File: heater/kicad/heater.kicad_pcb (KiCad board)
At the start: 2 copper layers, 90 x 88.4 mm, 117 parts, among them J1 Conn_01x07_Pin, J2 Conn_01x02_Pin, J3 Conn_01x02_Pin, J4 Conn_01x02_Pin, J5 pcie_98, U1 ADS1261BIRHBT, U2 ESD5344D-TP, U3 TPS7A2050PDBVR, U4 TPS7A2025PDBVRr, U6 TPS65135, U7 ADP7182AUJZ-5.0, U8 ADP7182AUJZ-2.5, U9 XC6206P332MR

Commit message: Heater PCB layout in progress.
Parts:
- removed C19: 220n, Capacitor_SMD:C_0402_1005Metric
- removed C22, C29, C32, C33, C37, C40, C41, C42, C47, C48: 10u, Capacitor_SMD:C_0603_1608Metric
- removed C23, C24, C25, C30, C31, C34, C36, C38, C39, C43, C44: 100n, Capacitor_SMD:C_0402_1005Metric
- removed C35, C45, C46: 1u, Capacitor_SMD:C_0402_1005Metric
- removed D3, D4: GRN, LED_SMD:LED_0603_1608Metric
- removed J3, J4: Conn_01x02_Pin, heater:connector_2pins_horizontal
- removed JP1, JP2: SolderJumper_2_Bridged, Jumper:SolderJumper-2_P1.3mm_Bridged_Pad1.0x1.5mm
- removed L1: 2u2H, heater:Inductor_C329578
- removed R1, R12, R2, R30, R36, R37, R38, R39, R40, R41, R42: 2K 0.1%, Resistor_SMD:R_0402_1005Metric
- removed R11, R20, R34, R5, R6: 1K, Resistor_SMD:R_0402_1005Metric
- removed R18, R19, R21: 47R, Resistor_SMD:R_0402_1005Metric
- removed R23, R24: 10K, Resistor_SMD:R_0402_1005Metric
- removed R25, R26: 5K1, Resistor_SMD:R_0402_1005Metric
- removed R28, R29: 51K, Resistor_SMD:R_0402_1005Metric
- removed R31: 360K 1%, Resistor_SMD:R_0402_1005Metric
- removed R32: 100K 1%, Resistor_SMD:R_0402_1005Metric
- removed R33: 464K 1%, Resistor_SMD:R_0402_1005Metric
- removed TP6: TestPoint, common:Test_Pad
- removed U6: TPS65135, heater:WQFN-16-1EP_3x3mm_P0.5mm_EP1.68x1.68mm_ThermalVias
- added R14: 0R, Resistor_SMD:R_0402_1005Metric, F.Cu at (77.4, -44.4)
- added R17: 30K, Resistor_SMD:R_0402_1005Metric, F.Cu at (77.4, -38.4)
- added TP10: TestPoint, common:Test_Pad, F.Cu at (83.2, -38.1)
- added TP11: TestPoint, common:Test_Pad, F.Cu at (83.2, -35.2)
- added TP12: TestPoint, common:Test_Pad, F.Cu at (86.1, -43.9)
- added TP13: TestPoint, common:Test_Pad, F.Cu at (86.1, -41.0)
- added TP14: TestPoint, common:Test_Pad, F.Cu at (86.1, -38.1)
- added U14: OPA863DBVR, heater:SOT-23-5, F.Cu at (70.4, -48.1)
- added U16: OPA863DBVR, heater:SOT-23-5, F.Cu at (70.4, -43.6)
- added U5: ISO1541, Package_SO:SOIC-8_3.9x4.9mm_P1.27mm, F.Cu at (91.8, -32.3)
- C1: value 2u2 -> 10u; footprint Capacitor_SMD:C_0402_1005Metric -> Capacitor_SMD:C_0603_1608Metric
- C10, C11: value 1u -> 100n
- C13: value 100n -> 2u2; footprint Capacitor_SMD:C_0402_1005Metric -> Capacitor_SMD:C_0805_2012Metric
- C14: value 22n -> 10u; footprint Capacitor_SMD:C_0402_1005Metric -> Capacitor_SMD:C_0603_1608Metric
- C15: value 220n -> 100n
- C16, C18: value 22n -> 100n
- C17: value 4n7 -> 100n
- C20: value 22n -> 10n
- C21: value 1u -> 10u; footprint Capacitor_SMD:C_0402_1005Metric -> Capacitor_SMD:C_0603_1608Metric
- C26: value 10u -> 10u 16V
- C4: value 100n -> 10u; footprint Capacitor_SMD:C_0402_1005Metric -> Capacitor_SMD:C_0603_1608Metric
- C5: footprint Capacitor_SMD:C_0402_1005Metric -> Capacitor_SMD:C_0805_2012Metric
- C6: value 2u2 -> 100n
- C9: value 100n -> 10u 16V; footprint Capacitor_SMD:C_0402_1005Metric -> Capacitor_SMD:C_0603_1608Metric
- D1: value GRN -> RED
- D2: value GRN -> YEL
- J1: value Conn_01x07_Pin -> Conn_01x02_Pin; footprint heater:connector_7pins_horizontal -> Connector_JST:JST_VH_B2PS-VH_1x02_P3.96mm_Horizontal
- J2: footprint heater:connector_2pins_horizontal -> Connector_JST:JST_VH_B2PS-VH_1x02_P3.96mm_Horizontal
- R10, R9: value 1K -> 1K8
- R13: value 2K 0.1% -> 0R
- R15: value 51K -> 3K3
- R16: value 51K -> 0R
- R22: value 47R -> 5K1
- R3: value 2K 0.1% -> 30K
- R4: value 1K -> 0R025 50ppm 3W; footprint Resistor_SMD:R_0402_1005Metric -> Resistor_SMD:R_2512_6332Metric
- R7, R8: value 2K 0.1% -> 1K8
- U1: value ADS1261BIRHBT -> OPA863DBVR; footprint heater:RHB0032E -> heater:SOT-23-5
- U3: value TPS7A2050PDBVR -> LP2985-5.0; footprint heater:SOT-23-5 -> Package_TO_SOT_SMD:SOT-23-5
- U4: value TPS7A2025PDBVRr -> ESD5344D-TP; footprint heater:SOT-23-5 -> common:Diodes_UDFN-10_1.0x2.5mm_P0.5mm
- U7: value ADP7182AUJZ-5.0 -> OPA863DBVR; footprint Package_TO_SOT_SMD:TSOT-23-5 -> heater:SOT-23-5
- U8: value ADP7182AUJZ-2.5 -> ADS1115IDGS; footprint Package_TO_SOT_SMD:TSOT-23-5 -> Package_SO:TSSOP-10_3x3mm_P0.5mm
- U9: footprint Package_TO_SOT_SMD:SOT-23-3 -> Package_TO_SOT_SMD:SOT-89-3
- moved D2 121.5 mm to (98.2, -38.0), turned to 0 degrees
- moved TP8 105.5 mm to (83.2, -43.9)
- moved U8 100.6 mm to (82.3, -31.4), turned to 0 degrees
- moved TP2 95.8 mm to (80.3, -43.9)
- moved U9 95.8 mm to (99.4, -32.5), turned to 0 degrees
- moved C18 92.5 mm to (94.7, -42.4), turned to 0 degrees
- moved TP4 92.4 mm to (80.3, -38.1)
- moved TP5 90.5 mm to (80.3, -35.2)
- moved C17 90.1 mm to (94.7, -44.4), turned to 0 degrees
- moved C15 89.9 mm to (91.8, -38.5)
- moved C12 89.3 mm to (91.8, -40.4), turned to 0 degrees
- moved C10 89.3 mm to (91.8, -44.4), turned to 0 degrees
- moved C16 89.1 mm to (91.8, -36.5), turned to 0 degrees
- moved C20 88.5 mm to (94.7, -40.4), turned to 0 degrees
- moved C14 88.1 mm to (94.8, -54.9), turned to 0 degrees
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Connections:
- C1 pad 1: /AIN6 -> GND
- C1 pad 2: /AIN7 -> +5V
- C10 pad 2: /+2V5A -> +3V3
- C11 pad 1: /+3V3D -> +5VF
- C11 pad 2: GND -> GND1
- C12 pad 1: GND -> +5VF
- C12 pad 2: /+2V5A -> GND1
- C13 pad 1: /+3V3D -> GND1
- C13 pad 2: GND -> Net-(U6-OUT)
- C14 pad 1: /AIN2 -> GND
- C14 pad 2: GND -> +5V
- C15 pad 1: /AIN0 -> +5VF
- C15 pad 2: /AIN1 -> GND1
- C16 pad 1: GND -> +5VF
- C16 pad 2: /AIN1 -> GND1
- C17 pad 1: Net-(U1-CAPN) -> +5VF
- C17 pad 2: Net-(U1-CAPP) -> GND1
- C18 pad 1: /AIN0 -> GND
- C18 pad 2: GND -> +5V
- C2 pad 2: /AIN6 -> +5V
- C20 pad 1: GND -> GND1
- C20 pad 2: /AIN3 -> Net-(U3-BP)
- C21 pad 1: Net-(U1-BYPASS) -> GND1
- C21 pad 2: GND -> +5VF
- C26 pad 1: GND -> GND1
- C26 pad 2: /+5VA -> /9VF
- C27 pad 1: GND -> GND1
- C27 pad 2: /+2V5A -> +5VF
- C28 pad 1: GND -> GND1
- C28 pad 2: /+2V5A -> +5VF
- C3 pad 2: /AIN4 -> +3V3
- C4 pad 1: /AIN7 -> GND
- C4 pad 2: GND -> +3V3
- C5 pad 1: /AIN8 -> GND1
- C5 pad 2: /AIN9 -> Net-(U15-OUT)
- C6 pad 1: /AIN4 -> +5VF
- C6 pad 2: /AIN5 -> GND1
- C7 pad 1: GND -> +5VF
- C7 pad 2: /AIN8 -> GND1
- C8 pad 1: /AIN9 -> +5VF
- C8 pad 2: GND -> GND1
- C9 pad 1: /AIN5 -> GND1
- C9 pad 2: GND -> /9VF
- D1 pad 1: GND -> Net-(D1-K)
- D1 pad 2: Net-(D1-A) -> +5VF
- D2 pad 1: Net-(D2-K) -> GND
- D2 pad 2: GND -> Net-(D2-A)
- D5 pad 1: GND -> GND1
- J1 pad 1: /-5VA -> GND1
- J2 pad 2: Net-(J2-Pin_2) -> Net-(J1-Pin_2)
- J5 pad A16: /PB14 -> unconnected-(J5-Pin_a16-PadA16)
- J5 pad A27: /PA7 -> unconnected-(J5-Pin_a27-PadA27)
- J5 pad B1: +5VD -> +5V
- J5 pad B10: unconnected-(J5-Pin_b10-PadB10) -> /PB7
- J5 pad B12: unconnected-(J5-Pin_b12-PadB12) -> /PB8
- J5 pad B2: +5VD -> +5V
- J5 pad B21: /PA6 -> unconnected-(J5-Pin_b21-PadB21)
- J5 pad B28: /PA5 -> unconnected-(J5-Pin_b28-PadB28)
- J5 pad B3: +5VD -> +5V
- J5 pad B4: +5VD -> +5V
- R10 pad 1: Net-(J4-Pin_2) -> /PB8
- R10 pad 2: /AIN8 -> +3V3
- R13 pad 1: /AIN0 -> Net-(U8-ADDR)
- R13 pad 2: Net-(J1-Pin_6) -> Net-(U5-SCL2)
- R15 pad 1: /PA6 -> +3V3
- R15 pad 2: /+3V3D -> Net-(D2-A)
- R16 pad 1: /PB14 -> Net-(U8-ADDR)
- R16 pad 2: /+3V3D -> GND1
- R22 pad 1: /PB14 -> Net-(R22-Pad1)
- R22 pad 2: Net-(U1-CS_N) -> Net-(D1-K)
- R27 pad 1: /+3V3D -> +5VF
- R3 pad 1: Net-(J2-Pin_2) -> Net-(U16--)
- R3 pad 2: /+2V5A -> Net-(U8-AIN1)
- R4 pad 1: Net-(J3-Pin_2) -> GND1
- R4 pad 2: /AIN6 -> Net-(J2-Pin_1)
- R7 pad 1: Net-(J4-Pin_2) -> Net-(U5-SDA2)
- R7 pad 2: /+2V5A -> +5VF
- R8 pad 1: /-2V5A -> Net-(U5-SCL2)
- R8 pad 2: Net-(J4-Pin_1) -> +5VF
- R9 pad 1: Net-(J2-Pin_1) -> /PB7
- R9 pad 2: /AIN5 -> +3V3
- TP2 pad 1: +5VD -> +3V3
- TP3 pad 1: /+5V7 -> Net-(U8-AIN1)
- TP4 pad 1: /-5V7 -> /9VF
- TP5 pad 1: /+5VA -> Net-(U15-OUT)
- TP7 pad 1: /+2V5A -> +5VF
- TP8 pad 1: /-2V5A -> Net-(U14-+)
- TP9 pad 1: /+3V3D -> Net-(R22-Pad1)
- U1 pad 1: GND -> Net-(R22-Pad1)
- U1 pad 2: Net-(U1-CAPP) -> GND1
- U1 pad 3: Net-(U1-CAPN) -> Net-(U1-+)
- U1 pad 4: /+2V5A -> Net-(U1--)
- U1 pad 5: /-2V5A -> +5VF
- U2 pad 1: /PB14 -> /PB7
- U2 pad 2: /PA6 -> unconnected-(U2-D2-Pad2)
- U2 pad 4: /PA7 -> unconnected-(U2-D3-Pad4)
- U2 pad 5: /PA5 -> /PB8
- U3 pad 1: /+5V7 -> /9VF
- U3 pad 2: GND -> GND1
- U3 pad 3: /+5V7 -> /9VF
- U3 pad 4: unconnected-(U3-NC-Pad4) -> Net-(U3-BP)
- U3 pad 5: /+5VA -> +5VF
- U4 pad 1: /+5VA -> +5V
- U4 pad 2: GND -> +5V
- U4 pad 3: /+5VA -> GND
- U4 pad 5: /+2V5A -> unconnected-(U4-D4-Pad5)
- U7 pad 1: GND -> Net-(U8-AIN0)
- U7 pad 2: /-5V7 -> GND1
- U7 pad 3: /-5V7 -> Net-(U6-OUT)
- U7 pad 4: unconnected-(U7-NC-Pad4) -> Net-(U7--)
- U7 pad 5: /-5VA -> +5VF
- U8 pad 1: GND -> Net-(U8-ADDR)
- U8 pad 2: /-5VA -> unconnected-(U8-RDY-Pad2)
- U8 pad 3: /-5VA -> GND1
- U8 pad 4: unconnected-(U8-NC-Pad4) -> Net-(U8-AIN0)
- U8 pad 5: /-2V5A -> Net-(U8-AIN1)
- U9 pad 2: /+3V3D -> +3V3
- U9 pad 3: +5VD -> +5V
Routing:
- net /-2V5A: track 151.7 -> 0.00 mm, vias 8 -> 0
- net /+2V5A: track 145.5 -> 0.00 mm, vias 3 -> 0
- net /+3V3D: track 142.6 -> 0.00 mm, vias 4 -> 0
- net /-5VA: track 99.1 -> 0.00 mm, vias 2 -> 0
- net +5VD: track 93.2 -> 0.00 mm
- net GND: track 121.2 -> 32.8 mm, vias 45 -> 0
- net /+5VA: track 76.4 -> 0.00 mm, vias 2 -> 0
- net /PA5: track 62.3 -> 0.00 mm, vias 2 -> 0
- net /PA7: track 60.7 -> 0.00 mm, vias 3 -> 0
- net /PA6: track 60.2 -> 0.00 mm, vias 2 -> 0
- net /PB14: track 56.2 -> 0.00 mm, vias 1 -> 0
- net /AIN9: track 43.5 -> 0.00 mm
- net /AIN8: track 42.0 -> 0.00 mm
- net /+5V7: track 41.4 -> 0.00 mm
- net /-5V7: track 36.1 -> 0.00 mm, vias 2 -> 0
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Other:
- board text added: "PWM POWER VER 0.2"
- board text added: "locked"
- board text removed: "+2.5VA"
- board text removed: "+2V5A"
- board text removed: "+3.3VD"
- board text removed: "+3V3"
- board text removed: "+5.7V"
- board text removed: "+5VA"
- board text removed: "+5VD"
- board text removed: "-2.5VA"
- board text removed: "-2V5A"
- board text removed: "-5.7V"
- board text removed: "-5VA"
- board text removed: "ADC VER 0.2"
- board text removed: "LOAD CELL"

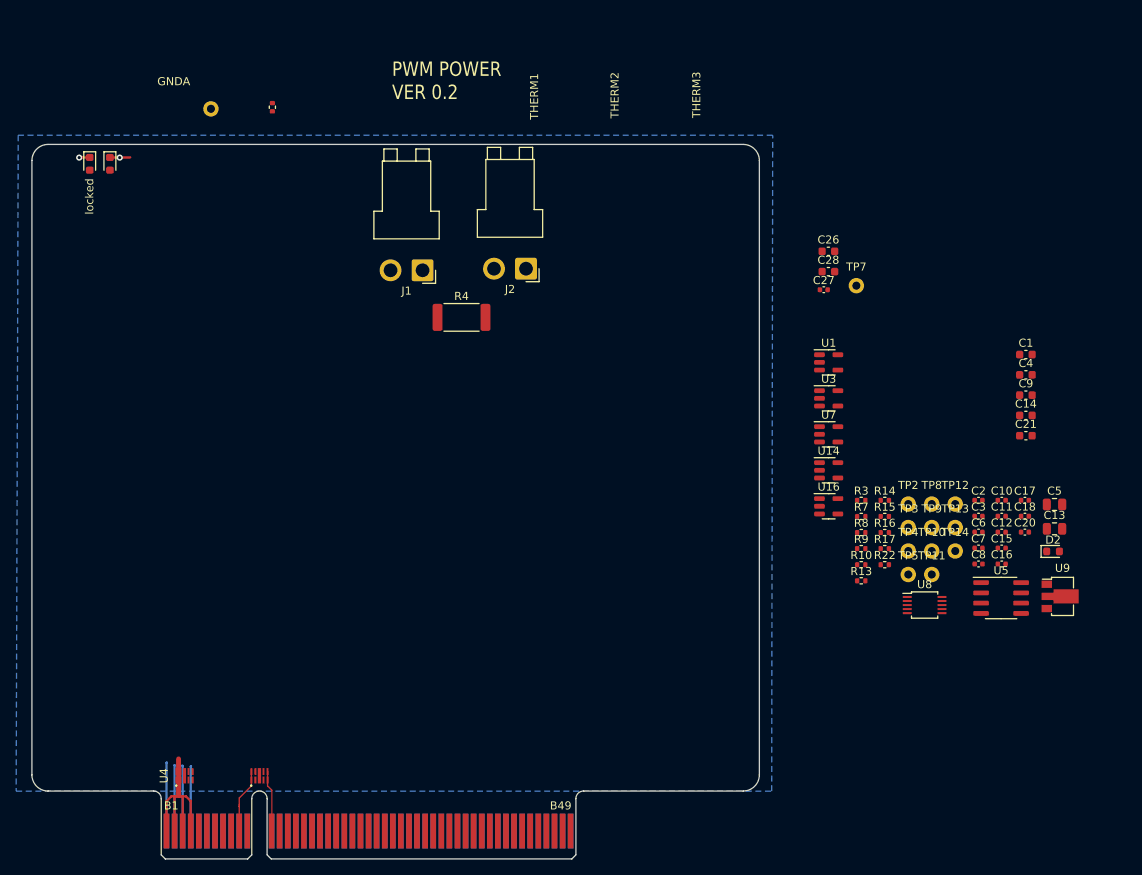
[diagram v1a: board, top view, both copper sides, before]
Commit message: Heater layout work in progress.
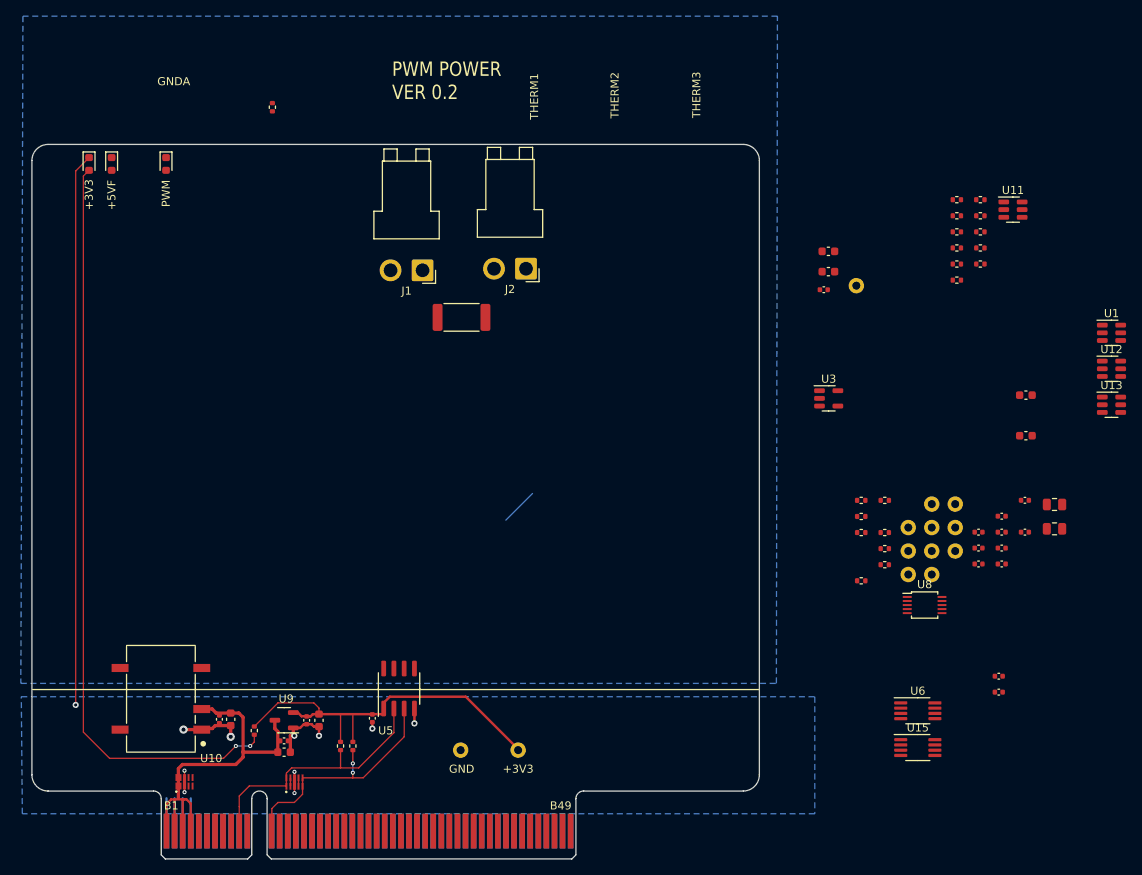
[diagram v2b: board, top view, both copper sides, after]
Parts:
- removed U14, U16, U7: OPA863DBVR, heater:SOT-23-5
- added C19: 100n 16V, Capacitor_SMD:C_0402_1005Metric, F.Cu at (91.5, -22.6)
- added C24: 100n 16V, Capacitor_SMD:C_0402_1005Metric, F.Cu at (91.5, -20.6)
- added R1: 10K, Resistor_SMD:R_0402_1005Metric, F.Cu at (86.3, -81.6)
- added R11: 50K, Resistor_SMD:R_0402_1005Metric, F.Cu at (86.3, -73.6)
- added R12: 2K, Resistor_SMD:R_0402_1005Metric, F.Cu at (86.3, -71.6)
- added R18: 10K, Resistor_SMD:R_0402_1005Metric, F.Cu at (89.2, -81.6)
- added R19: 100k, Resistor_SMD:R_0402_1005Metric, F.Cu at (89.2, -79.6)
- added R2: 1K, Resistor_SMD:R_0402_1005Metric, F.Cu at (86.3, -79.6)
- added R20: 3K3, Resistor_SMD:R_0402_1005Metric, F.Cu at (89.2, -77.6)
- added R21: 10K, Resistor_SMD:R_0402_1005Metric, F.Cu at (89.2, -75.6)
- added R24: 1M, Resistor_SMD:R_0402_1005Metric, F.Cu at (89.2, -73.6)
- added R5: 10K, Resistor_SMD:R_0402_1005Metric, F.Cu at (86.3, -77.6)
- added R6: 0R, Resistor_SMD:R_0402_1005Metric, F.Cu at (86.3, -75.6)
- added U10: B0509XT-1WR3, heater:Converter_DCDC, F.Cu at (-12.2, -19.8)
- added U11: OPA863SIDBVR, Package_TO_SOT_SMD:TSOT-23-6, F.Cu at (93.2, -80.3)
- added U12: OPA863SIDBVR, Package_TO_SOT_SMD:TSOT-23-6, F.Cu at (105.4, -60.6)
- added U13: OPA863SIDBVR, Package_TO_SOT_SMD:TSOT-23-6, F.Cu at (105.4, -56.2)
- added U15: LTC1968, Package_SO:MSOP-8_3x3mm_P0.65mm, F.Cu at (81.5, -13.8)
- added U6: LTC1968, Package_SO:MSOP-8_3x3mm_P0.65mm, F.Cu at (81.5, -18.3)
- D2: value YEL -> GRN
- J1, J2: footprint Connector_JST:JST_VH_B2PS-VH_1x02_P3.96mm_Horizontal -> heater:JST_VH_B2PS-VH_1x02_P3.96mm_Horizontal
- U1: value OPA863DBVR -> OPA863SIDBVR; footprint heater:SOT-23-5 -> Package_TO_SOT_SMD:TSOT-23-6
- U9: footprint Package_TO_SOT_SMD:SOT-89-3 -> heater:SOT-23-3
- moved D2 128.5 mm to (-21.1, -86.0), turned to -90 degrees
- moved C14 105.3 mm to (-3.56, -17.3), turned to 90 degrees
- moved C1 104.1 mm to (3.05, -13.2), turned to 180 degrees
- moved C18 102.8 mm to (-4.95, -17.3), turned to 90 degrees
- moved U9 97.5 mm to (3.05, -17.2), turned to 180 degrees
- moved C4 97.3 mm to (7.37, -17.1), turned to 90 degrees
- moved C2 90.9 mm to (3.05, -14.6), turned to 180 degrees
- moved C3 86.9 mm to (5.84, -17.1), turned to 90 degrees
- moved TP1 85.1 mm to (24.9, -13.5)
- moved C10 82.4 mm to (14.0, -17.4), turned to 90 degrees
- moved R15 82.4 mm to (-0.64, -15.9), turned to -90 degrees
- moved U5 75.3 mm to (17.3, -21.1), turned to 90 degrees
- moved R9 68.9 mm to (10.0, -14.0), turned to 90 degrees
- moved R10 66.8 mm to (11.6, -14.0), turned to 90 degrees
- moved TP2 57.1 mm to (32.0, -13.5)
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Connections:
- net GND1 renamed GNDF
- TP12 pad 1: Net-(U1--) -> Net-(U11--)
- TP8 pad 1: Net-(U14-+) -> Net-(U1-+)
- U1 pad 1: Net-(R22-Pad1) -> Net-(R1-Pad1)
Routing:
- net Net-(D2-A): track 0.00 -> 94.0 mm, vias 0 -> 2
- net GND: track 32.8 -> 107.9 mm, vias 0 -> 11
- net +3V3: track 0.00 -> 49.1 mm
- net /PB7: track 8.28 -> 32.9 mm
- net +5V: track 24.9 -> 49.6 mm
- net /PB8: track 7.58 -> 30.9 mm, vias 0 -> 2
- net GNDF: track 1.28 -> 4.67 mm, vias 1 -> 0
- net Net-(D1-K): track 2.50 -> 0.00 mm, vias 1 -> 0
- net unconnected-(U2-D3-Pad4): track 0.00 -> 1.05 mm
- net unconnected-(U2-D2-Pad2): track 0.00 -> 1.05 mm
- added copper zone on B.Cu, net GNDF
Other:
- board text added: "+3V3"
- board text added: "+5VF"
- board text added: "GND"
- board text added: "PWM"
- board text removed: "locked"

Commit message: More progress with the heater layout.
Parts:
- J1, J2: footprint heater:JST_VH_B2PS-VH_1x02_P3.96mm_Horizontal -> heater:JST_VH_2_CHINESE
- moved C9 110.3 mm to (-11.8, -29.2), turned to 180 degrees
- moved C24 104.3 mm to (-11.8, -35.4), turned to 180 degrees
- moved C20 103.8 mm to (-9.02, -37.8), turned to -90 degrees
- moved C19 103.4 mm to (-11.8, -27.6), turned to 180 degrees
- moved U13 98.4 mm to (7.11, -61.3)
- moved R22 98.0 mm to (-11.4, -78.0), turned to 90 degrees
- moved TP4 96.4 mm to (-16.1, -38.4)
- moved U11 96.2 mm to (-2.54, -70.9)
- moved C11 96.2 mm to (0.13, -71.5), turned to -90 degrees
- moved R24 95.1 mm to (-5.84, -70.9), turned to 90 degrees
- moved C13 94.8 mm to (7.11, -66.4)
- moved C26 91.9 mm to (-11.7, -33.9), turned to 180 degrees
- moved U6 90.3 mm to (7.16, -69.6)
- moved R12 89.9 mm to (-3.56, -68.5)
- moved TP7 88.1 mm to (-10.8, -46.4)
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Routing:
- net GNDF: track 4.67 -> 92.4 mm, vias 0 -> 24
- net +5VF: track 0.00 -> 60.3 mm
- net Net-(U5-SCL2): track 0.00 -> 44.7 mm
- net Net-(U5-SDA2): track 0.00 -> 34.1 mm
- net Net-(J1-Pin_2): track 0.00 -> 24.2 mm
- net /9VF: track 0.00 -> 22.0 mm
- net Net-(U8-AIN1): track 0.00 -> 18.2 mm
- net Net-(U8-AIN0): track 0.00 -> 15.3 mm
- net Net-(U11--): track 0.00 -> 15.1 mm
- net Net-(J2-Pin_1): track 0.00 -> 13.0 mm
- net Net-(R22-Pad1): track 0.00 -> 10.8 mm
- net Net-(U13-+): track 0.00 -> 10.1 mm
- net Net-(U12-+): track 0.00 -> 9.03 mm
- net Net-(U8-ADDR): track 0.00 -> 8.97 mm
- net Net-(D1-K): track 0.00 -> 8.81 mm
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
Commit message: More progress with the heatrer layout
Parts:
- moved C20 20.3 mm to (1.65, -55.1)
- moved TP7 20.3 mm to (-0.13, -63.6)
- moved U3 20.3 mm to (-1.14, -55.1)
- moved TP4 20.3 mm to (-5.46, -55.6)
- moved C24 20.3 mm to (-1.14, -52.7)
- moved C26 20.3 mm to (-1.02, -51.2)
- moved C27 20.3 mm to (-1.04, -57.5)
- moved C28 20.3 mm to (-1.14, -58.9)
- moved D1 17.3 mm to (5.71, -86.0)
- moved R22 17.3 mm to (5.84, -78.0)
- moved C15 15.3 mm to (25.4, -54.6)
- moved R13 15.3 mm to (15.6, -55.9)
- moved R14 15.3 mm to (15.6, -57.9)
- moved R16 15.3 mm to (15.6, -53.7)
- moved U8 15.3 mm to (21.7, -55.1)
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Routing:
- net Net-(U8-AIN1): track 18.2 -> 28.0 mm
- net Net-(J1-Pin_2): track 24.2 -> 20.9 mm
- net GNDF: track 92.4 -> 89.2 mm
- net Net-(U5-SCL2): track 44.7 -> 47.9 mm
- net Net-(U5-SDA2): track 34.1 -> 37.3 mm
- net Net-(U11--): track 15.1 -> 12.2 mm

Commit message: More progress with the heater layout.
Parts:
- added R23: 0R, Resistor_SMD:R_0402_1005Metric, F.Cu at (27.4, -74.3)
- moved TP4 24.2 mm to (-15.6, -33.7)
- moved R8 9.32 mm to (35.8, -45.3), turned to -90 degrees
- moved R7 7.90 mm to (32.8, -45.3), turned to -90 degrees
- moved R4 5.72 mm to (27.4, -82.2), turned to 90 degrees
- moved R16 3.28 mm to (15.5, -57.0), turned to 180 degrees
- moved R13 2.94 mm to (15.5, -53.0), turned to 180 degrees
- moved R14 2.94 mm to (15.5, -55.0), turned to 180 degrees
- moved TP7 1.35 mm to (-1.02, -62.6)
- moved C11 1.25 mm to (12.2, -70.6)
- moved R24 1.11 mm to (6.35, -70.1)
- moved U11 1.11 mm to (9.65, -70.1)
- moved R21 1.10 mm to (33.5, -74.3)
- moved R11 1.10 mm to (10.8, -67.8)
- moved R12 1.10 mm to (8.64, -67.8)
- moved R6 0.62 mm to (30.2, -65.9)
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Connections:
- J1 pad 1: GNDF -> Net-(J1-Pin_1)
- R4 pad 1: GNDF -> Net-(J1-Pin_1)
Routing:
- net +5VF: track 60.3 -> 25.3 mm
- net Net-(J2-Pin_1): track 13.0 -> 37.2 mm
- net Net-(J1-Pin_1): track 0.00 -> 14.1 mm
- net Net-(U8-AIN1): track 28.0 -> 19.8 mm
- net Net-(J1-Pin_2): track 20.9 -> 26.3 mm
- net Net-(U5-SCL2): track 47.9 -> 53.1 mm
- net Net-(U8-AIN0): track 15.3 -> 12.3 mm
- net Net-(U11--): track 12.2 -> 14.9 mm
- net Net-(U5-SDA2): track 37.3 -> 35.3 mm
- net GNDF: track 89.2 -> 87.4 mm, vias 24 -> 27
- net Net-(U8-ADDR): track 8.97 -> 7.59 mm
- net Net-(U1-+): track 4.73 -> 6.03 mm
- net Net-(R22-Pad1): track 10.8 -> 9.87 mm
- net Net-(U12--): track 2.68 -> 3.45 mm
- net Net-(U13--): track 3.06 -> 3.77 mm
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- added copper zone on B.Cu, net (none)
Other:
- board text added: "CH1"
- board text added: "CH2"
- board text added: "CH3"
